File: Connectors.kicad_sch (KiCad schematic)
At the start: 14 parts, among them J1 A, J10 4900, J11 4900, J12 4900, J13 4900, J14 4900, J2 B, J3 C, J4 Conn_02x07_Odd_Even, J5 4900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

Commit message: VER2.0
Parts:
- removed J4: Conn_02x07_Odd_Even, Connector_PinSocket_2.54mm:PinSocket_2x07_P2.54mm_Vertical, symbol Connector_Generic:Conn_02x07_Odd_Even
- removed J8: Conn_02x02_Odd_Even, Connector_PinHeader_2.54mm:PinHeader_2x02_P2.54mm_Vertical, symbol Connector_Generic:Conn_02x02_Odd_Even
- added J14: 4900, Connector_My:4900, symbol 4900:4900
- added J15: Conn_02x04_Odd_Even, Connector_PinHeader_2.00mm:PinHeader_2x04_P2.00mm_Vertical, symbol Connector_Generic:Conn_02x04_Odd_Even
- added J8: Temp, Connector_PinHeader_2.54mm:PinHeader_1x03_P2.54mm_Vertical, symbol Connector:Conn_01x03_Socket
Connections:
- net +3.3VA: now also J15.7 (Pin_7)
- net Current_A_MCU: now also J15.5 (Pin_5)
- net Current_B_MCU: now also J15.3 (Pin_3)
- net Current_C_MCU: now also J15.1 (Pin_1)
- net GNDA: now also J15.8 (Pin_8), J8.3 (Pin_3)
- net OUT_MCU: now also J15.2 (Pin_2)
- net PTC_Coil_A: now also J8.1 (Pin_1)
- net PTC_Coil_B: now also J8.2 (Pin_2)
- net Temp_Coil_A_MCU: now also J15.6 (Pin_6)
- net Temp_Coil_B_MCU: now also J15.4 (Pin_4)
- net A renamed A+
- net A_OUT renamed A-
- net B renamed B+
- net B_OUT renamed B-
- net B-: now also J14.1, J14.2
- net C renamed C+
- net C_OUT renamed C-

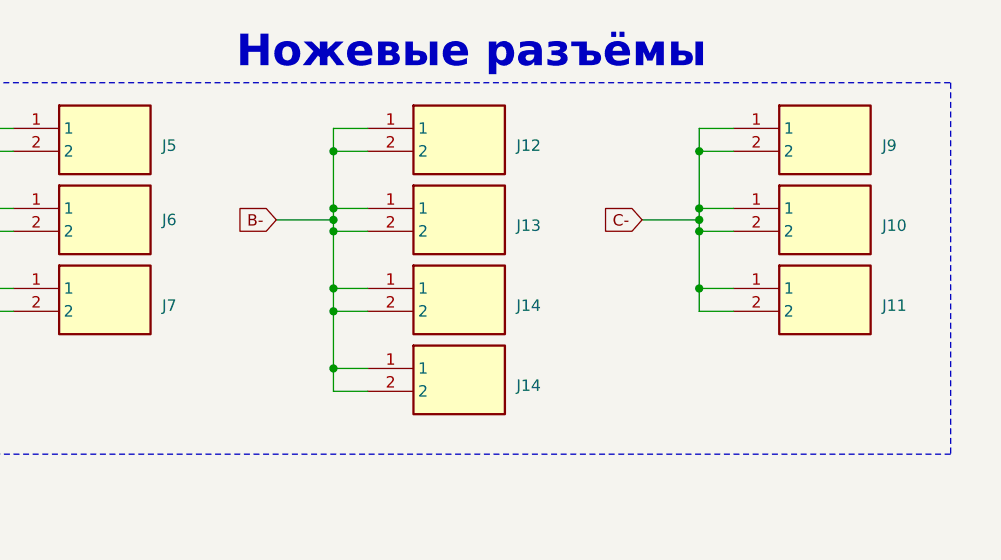
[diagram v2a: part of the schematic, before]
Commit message: Убрал лишние шунты
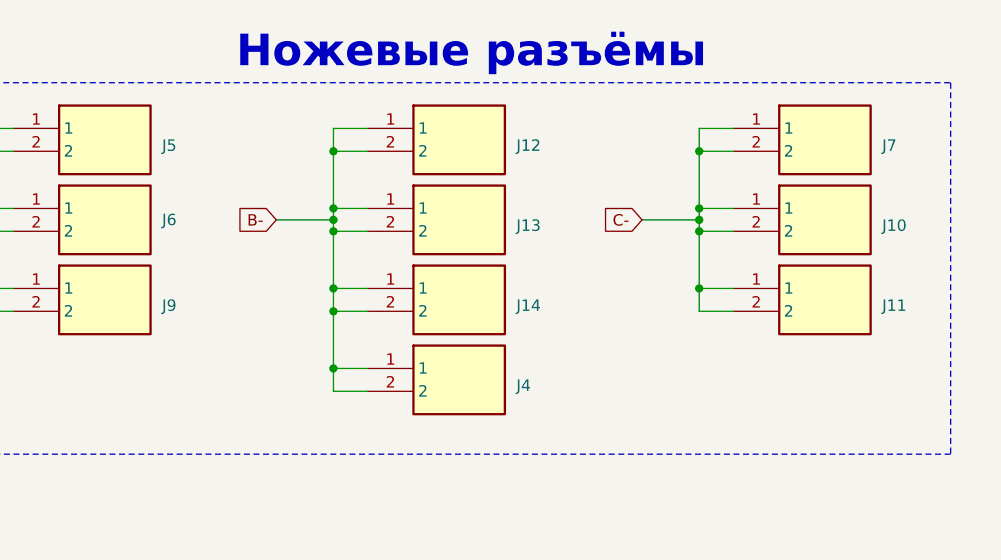
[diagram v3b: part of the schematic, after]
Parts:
- J15: footprint Connector_PinHeader_2.00mm:PinHeader_2x04_P2.00mm_Vertical -> Connector_PinHeader_1.27mm:PinHeader_2x04_P1.27mm_Vertical
- renumbered J14 to J4, J9 to J7, J7 to J9

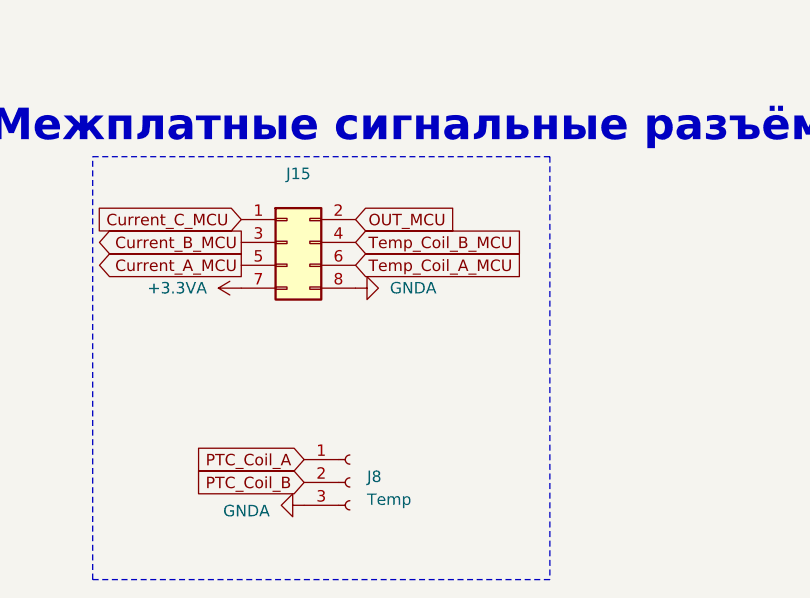
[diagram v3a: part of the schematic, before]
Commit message: Добавил разъёмы для крепления
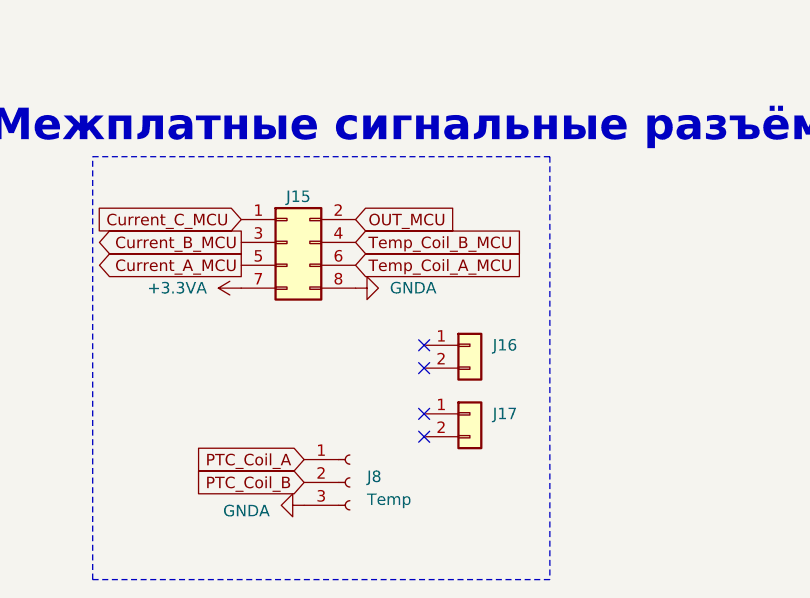
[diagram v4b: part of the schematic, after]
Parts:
- added J16, J17: Conn_01x02, Connector_PinHeader_1.27mm:PinHeader_1x02_P1.27mm_Vertical, symbol Connector_Generic:Conn_01x02
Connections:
- no-connect marks 0 -> 4
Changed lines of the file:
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@@
 		(color 0 0 0 0)
+	)
+	(no_connect
+		(at 81.28 161.29)
+	)
+	(no_connect
+		(at 81.28 151.13)
+	)
+	(no_connect
+		(at 81.28 158.75)
+	)
+	(no_connect
+		(at 81.28 153.67)
 	)
 	(wire
@@
 	)
 	(symbol
+		(lib_id "Connector_Generic:Conn_01x02")
+		(at 86.36 158.75 0)
+		(unit 1)
+		(exclude_from_sim no)
+		(in_bom yes)
+		(on_board yes)
+		(dnp no)
+		(fields_autoplaced yes)
+		(property "Reference" "J17"
+			(at 88.9 158.7499 0)
+			(effects
+				(font
+					(size 1.27 1.27)
+				)
+				(justify left)
+			)
+		)
+		(property "Value" "Conn_01x02"
+			(at 88.9 161.2899 0)
+			(effects
+				(font
+					(size 1.27 1.27)
+				)
+				(justify left)
+				(hide yes)
+			)
+		)
+		(property "Footprint" "Connector_PinHeader_1.27mm:PinHeader_1x02_P1.27mm_Vertical"
+			(at 86.36 158.75 0)
+			(effects
+				(font
+					(size 1.27 1.27)
+				)
+				(hide yes)
+			)
+		)
+		(property "Datasheet" "~"
+			(at 86.36 158.75 0)
+			(effects
+				(font
+					(size 1.27 1.27)
+				)
+				(hide yes)
+			)
+		)
+		(property "Description" "Generic connector, single row, 01x02, script generated (kicad-library-utils/schlib/autogen/connector/)"
+			(at 86.36 158.75 0)
+			(effects
+				(font
+					(size 1.27 1.27)
+				)
+				(hide yes)
+			)
+		)
+		(pin "1"
+		)
+		(pin "2"
+		)
+		(instances
+			(project "Плата датчиков"
+				(path "/69677e3f-3942-4c93-9a5c-92669e2df5eb/555e8538-1d60-4a85-8162-4c8254aec889"
+					(reference "J17")
+					(unit 1)
+				)
+			)
+		)
+	)
+	(symbol
 		(lib_id "4900:4900")
 		(at 204.47 87.63 0)
@@
 	)
 	(symbol
+		(lib_id "Connector_Generic:Conn_01x02")
+		(at 86.36 151.13 0)
+		(unit 1)
+		(exclude_from_sim no)
+		(in_bom yes)
+		(on_board yes)
+		(dnp no)
+		(fields_autoplaced yes)
+		(property "Reference" "J16"
+			(at 88.9 151.1299 0)
+			(effects
+				(font
+					(size 1.27 1.27)
+				)
+				(justify left)
+			)
+		)
+		(property "Value" "Conn_01x02"
+			(at 88.9 153.6699 0)
+			(effects
+				(font
+					(size 1.27 1.27)
+				)
+				(justify left)
+				(hide yes)
+			)
+		)
+		(property "Footprint" "Connector_PinHeader_1.27mm:PinHeader_1x02_P1.27mm_Vertical"
+			(at 86.36 151.13 0)
+			(effects
+				(font
+					(size 1.27 1.27)
+				)
+				(hide yes)
+			)
+		)
+		(property "Datasheet" "~"
+			(at 86.36 151.13 0)
+			(effects
+				(font
+					(size 1.27 1.27)
+				)
+				(hide yes)
+			)
+		)
+		(property "Description" "Generic connector, single row, 01x02, script generated (kicad-library-utils/schlib/autogen/connector/)"
+			(at 86.36 151.13 0)
+			(effects
+				(font
+					(size 1.27 1.27)
+				)
+				(hide yes)
+			)
+		)
+		(pin "1"
+		)
+		(pin "2"
+		)
+		(instances
+			(project "Плата датчиков"
+				(path "/69677e3f-3942-4c93-9a5c-92669e2df5eb/555e8538-1d60-4a85-8162-4c8254aec889"
+					(reference "J16")
+					(unit 1)
+				)
+			)
+		)
+	)
+	(symbol
 		(lib_id "Connector_Generic:Conn_01x01")
 		(at 86.995 80.01 0)
@@
 		(on_board yes)
 		(dnp no)
-		(fields_autoplaced yes)
 		(property "Reference" "J15"
-			(at 67.31 132.08 0)
-			(effects
-				(font
+			(at 67.31 134.62 0)
+			(effects
+				(font

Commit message: Отправил на проверку в резонит
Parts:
- removed J15: Conn_02x04_Odd_Even, Connector_PinHeader_1.27mm:PinHeader_2x04_P1.27mm_Vertical, symbol Connector_Generic:Conn_02x04_Odd_Even
- added J18: Conn_02x05_Odd_Even, Connector_PinHeader_1.27mm:PinHeader_2x05_P1.27mm_Vertical, symbol Connector_Generic:Conn_02x05_Odd_Even
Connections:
- net +3.3VA: now also J18.10 (Pin_10), J18.8 (Pin_8)
- net Current_A_MCU: now also J18.6 (Pin_6)
- net Current_B_MCU: now also J18.4 (Pin_4)
- net Current_C_MCU: now also J18.2 (Pin_2)
- net GNDA: now also J18.7 (Pin_7), J18.9 (Pin_9)
- net OUT_MCU: now also J18.1 (Pin_1)
- net Temp_Coil_A_MCU: now also J18.5 (Pin_5)
- net Temp_Coil_B_MCU: now also J18.3 (Pin_3)

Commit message: Изменения: добавил папку с отчетностью
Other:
- moved on the sheet: J1, J10, J11, J12, J13, J14, J16, J17, J18, J2, J3, J4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
